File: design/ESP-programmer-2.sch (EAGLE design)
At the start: 21 parts, among them J1 10118193-0001LF, Q2 ON_SEMICONDUCTOR_BC849BLT1GON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, Q3 ON_SEMICONDUCTOR_BC849BLT1GON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, U1 CP2104-F03-GM

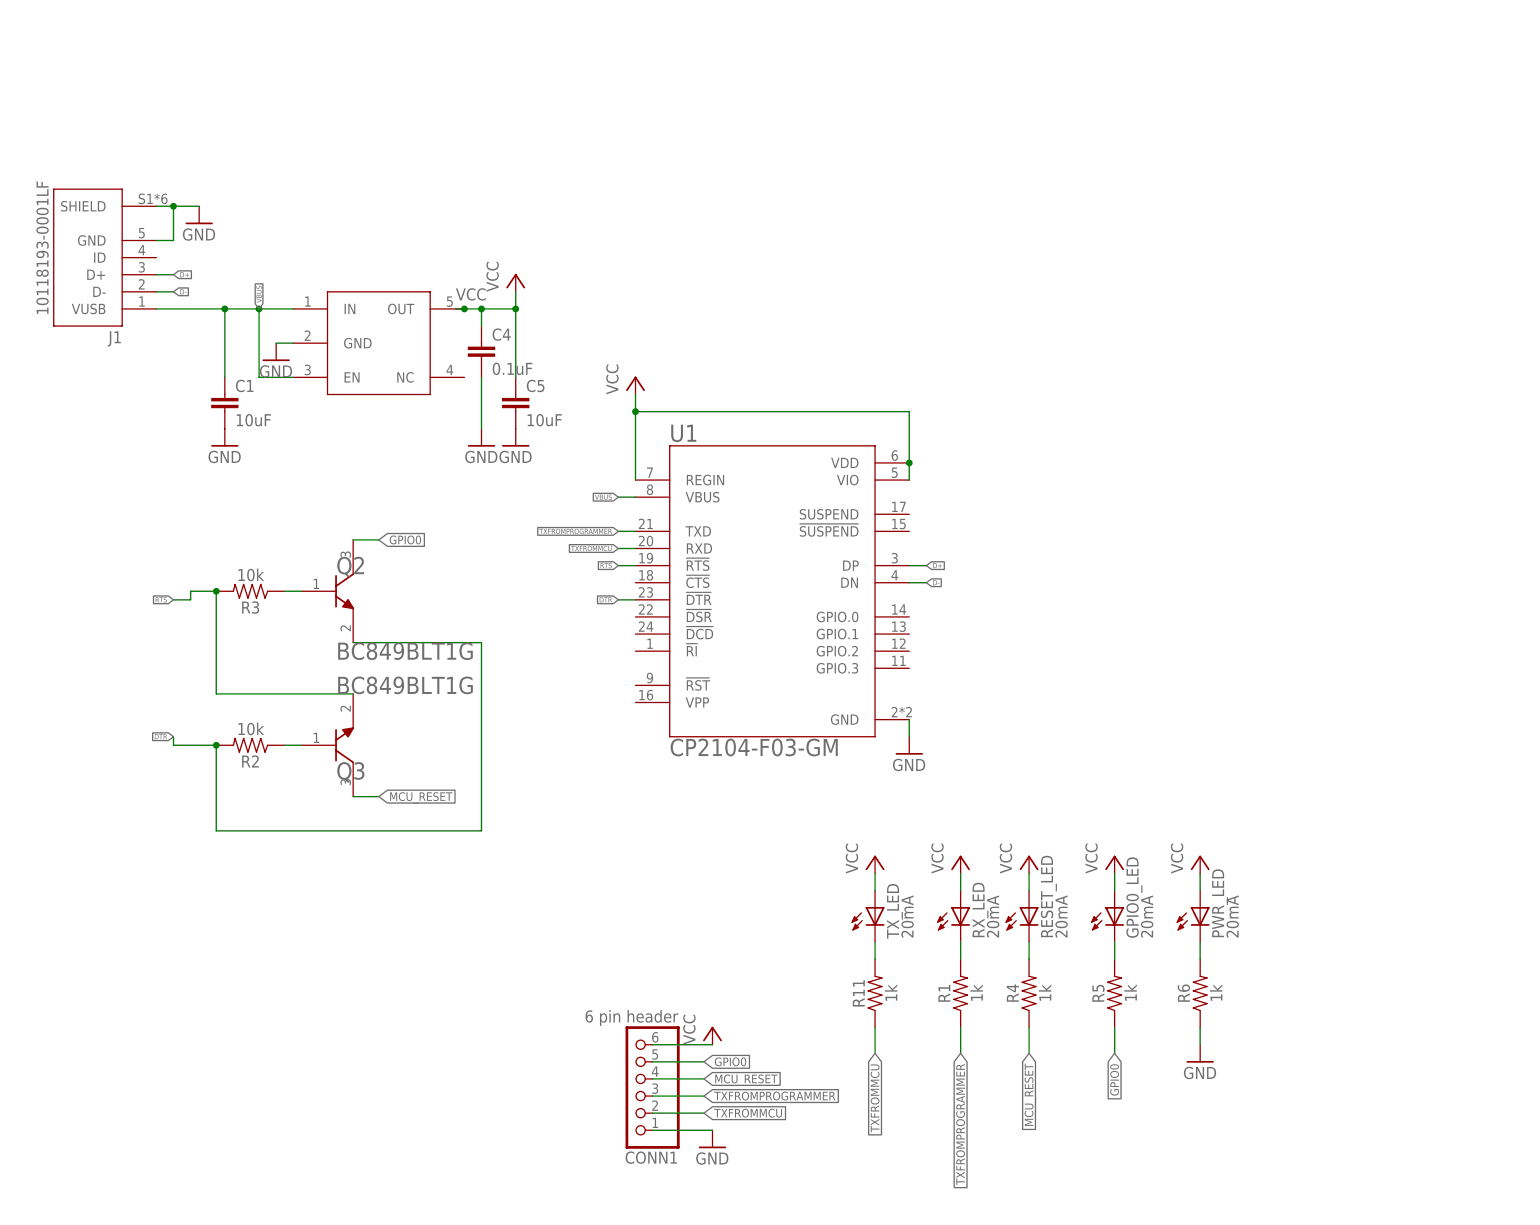
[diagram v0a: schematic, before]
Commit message: Added production and assembly files
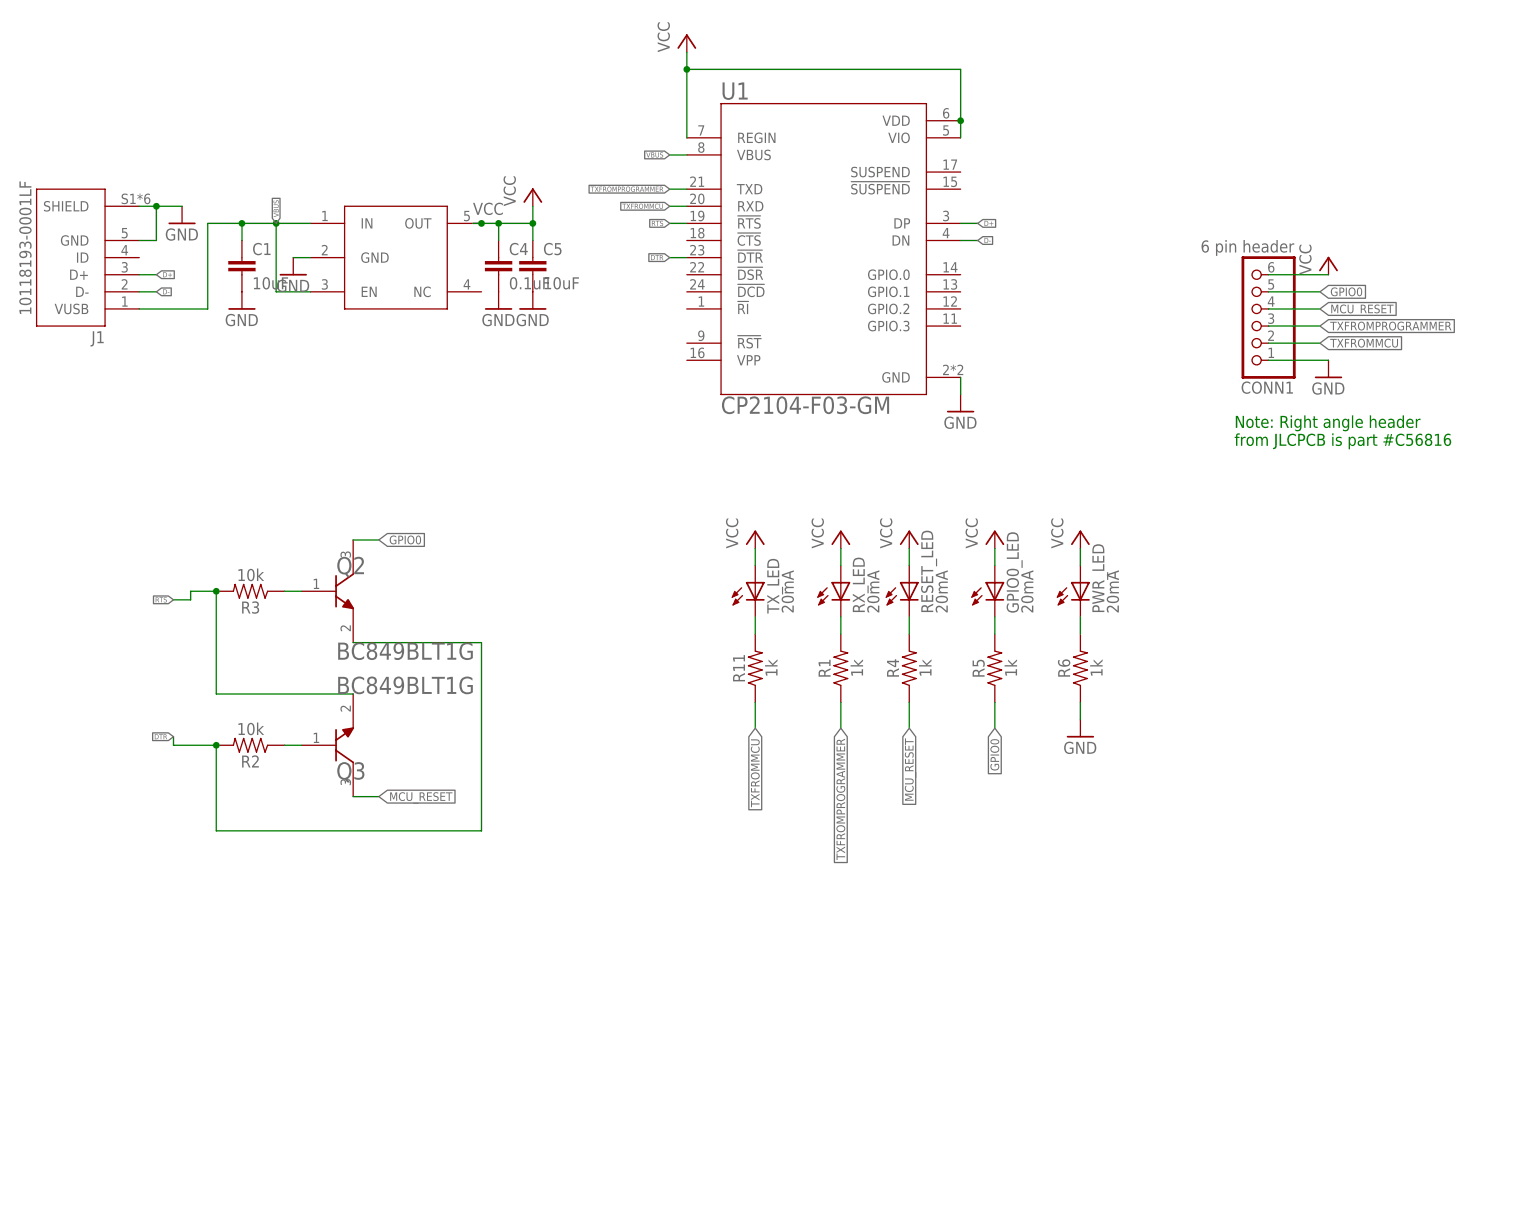
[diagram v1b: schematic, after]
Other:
- note added: "Note: Right angle header from JLCPCB is part #C56816"
- moved on the sheet: C1, C4, C5, CONN1, GPIO0_LED, J1, PWR_LED, R1, R11, R4, R5, R6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
